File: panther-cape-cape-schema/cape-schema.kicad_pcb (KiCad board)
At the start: 2 copper layers, 86.4 x 54.6 mm, 28 parts, among them P1 OUT2 P4, P10 Y_SENSORS, P11 SENSORS+, P12 SENSORS-, P13 SPINCLE_FEEDBACK, P14 SPINDLE, P15 Z_SENSORS, P16 DRIVER_ENABLE_SWITCH, P17 DRIVER_X, P18 DRIVER_Y, P19 DRIVER_Z, P2 IN2 P2, P20 DRIVER_ENABLE, P21 X_ALARM, P22 Y/Z_ALARM, P3 POWER_SUPPLY, P4 OUT1 P3, P5 EMERGENCY_STOP_SWITCH, P6 IN1 P1, P7 Z_PROBE_LIMIT_SWITCH, P8 X_SENSORS, P9 X_HOME

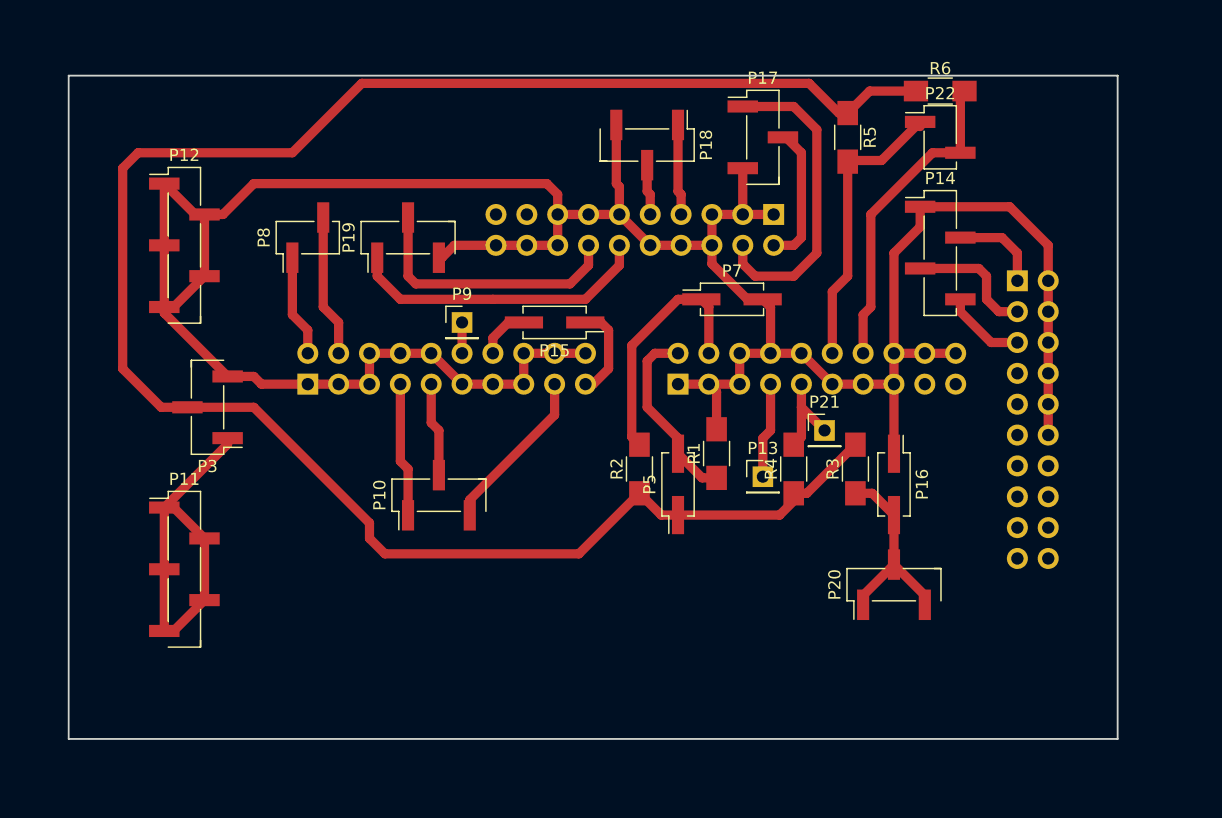
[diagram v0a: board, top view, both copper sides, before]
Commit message: routed single layer pcb
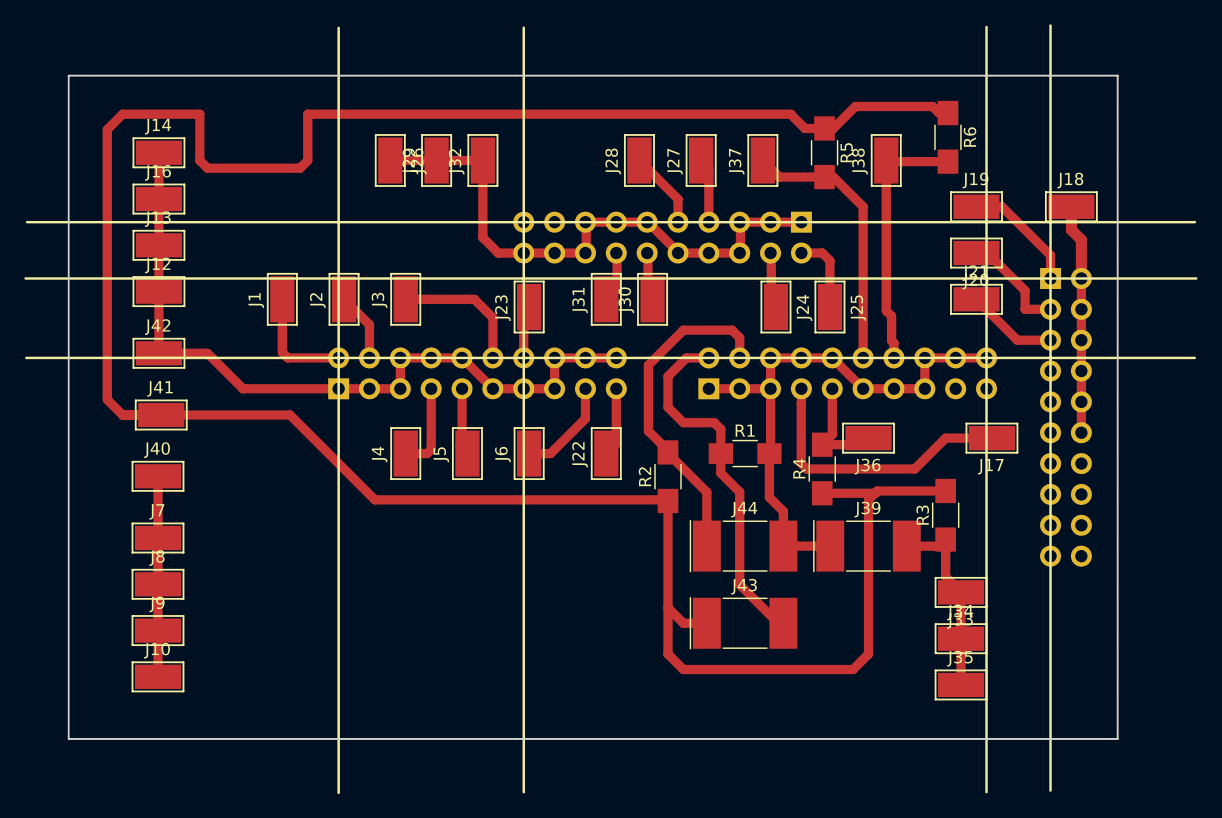
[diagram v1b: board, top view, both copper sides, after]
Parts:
- removed P10: Y_SENSORS, Pin_Headers:Pin_Header_Straight_1x03_Pitch2.54mm_SMD_Pin1Left
- removed P11: SENSORS+, Pin_Headers:Pin_Header_Straight_1x05_Pitch2.54mm_SMD_Pin1Left
- removed P12: SENSORS-, Pin_Headers:Pin_Header_Straight_1x05_Pitch2.54mm_SMD_Pin1Left
- removed P13: SPINCLE_FEEDBACK, Pin_Headers:Pin_Header_Straight_1x01_Pitch2.54mm
- removed P14: SPINDLE, Pin_Headers:Pin_Header_Straight_1x04_Pitch2.54mm_SMD_Pin1Left
- removed P15: Z_SENSORS, Pin_Headers:Pin_Header_Straight_2x01_Pitch2.54mm_SMD
- removed P16: DRIVER_ENABLE_SWITCH, Pin_Headers:Pin_Header_Straight_2x01_Pitch2.54mm_SMD
- removed P17: DRIVER_X, Pin_Headers:Pin_Header_Straight_1x03_Pitch2.54mm_SMD_Pin1Left
- removed P18: DRIVER_Y, Pin_Headers:Pin_Header_Straight_1x03_Pitch2.54mm_SMD_Pin1Left
- removed P19: DRIVER_Z, Pin_Headers:Pin_Header_Straight_1x03_Pitch2.54mm_SMD_Pin1Left
- removed P20: DRIVER_ENABLE, Pin_Headers:Pin_Header_Straight_1x03_Pitch2.54mm_SMD_Pin1Left
- removed P21: X_ALARM, Pin_Headers:Pin_Header_Straight_1x01_Pitch2.54mm
- removed P22: Y/Z_ALARM, Pin_Headers:Pin_Header_Straight_1x02_Pitch2.54mm_SMD_Pin1Left
- removed P3: POWER_SUPPLY, Pin_Headers:Pin_Header_Straight_1x03_Pitch2.54mm_SMD_Pin1Left
- removed P5: EMERGENCY_STOP_SWITCH, Pin_Headers:Pin_Header_Straight_2x01_Pitch2.54mm_SMD
- removed P7: Z_PROBE_LIMIT_SWITCH, Pin_Headers:Pin_Header_Straight_2x01_Pitch2.54mm_SMD
- removed P8: X_SENSORS, Pin_Headers:Pin_Header_Straight_1x02_Pitch2.54mm_SMD_Pin1Left
- removed P9: X_HOME, Pin_Headers:Pin_Header_Straight_1x01_Pitch2.54mm
- added J1: X_LIMIT_MIN, Measurement_Points:Test_Point_Keystone_5019_Minature, F.Cu at (46.2, 133.3)
- added J10: SENSORS+, Measurement_Points:Test_Point_Keystone_5019_Minature, F.Cu at (35.9, 164.4)
- added J12: SENSORS-, Measurement_Points:Test_Point_Keystone_5019_Minature, F.Cu at (36.0, 132.7)
- added J13: SENSORS-, Measurement_Points:Test_Point_Keystone_5019_Minature, F.Cu at (36.0, 128.9)
- added J14: SENSORS-, Measurement_Points:Test_Point_Keystone_5019_Minature, F.Cu at (36.0, 121.3)
- added J16: SENSORS-, Measurement_Points:Test_Point_Keystone_5019_Minature, F.Cu at (36.0, 125.1)
- added J17: SPINDLE_FEEDBACK, Measurement_Points:Test_Point_Keystone_5019_Minature, F.Cu at (104.6, 144.8)
- added J18: SPINDLE_SIGNAL-, Measurement_Points:Test_Point_Keystone_5019_Minature, F.Cu at (111.1, 125.7)
- added J19: SPINDLE_ENABLE, Measurement_Points:Test_Point_Keystone_5019_Minature, F.Cu at (103.3, 125.7)
- added J2: X_LIMIT_MAX, Measurement_Points:Test_Point_Keystone_5019_Minature, F.Cu at (51.2, 133.3)
- added J20: SPINDLE_DIR, Measurement_Points:Test_Point_Keystone_5019_Minature, F.Cu at (103.3, 129.5)
- added J21: SPINDLE_RPM, Measurement_Points:Test_Point_Keystone_5019_Minature, F.Cu at (103.3, 133.3)
- added J22: Z_LIMIT_MIN, Measurement_Points:Test_Point_Keystone_5019_Minature, F.Cu at (72.8, 146.1)
- added J23: Z_LIMIT_MAX, Measurement_Points:Test_Point_Keystone_5019_Minature, F.Cu at (66.5, 134.0)
- added J24: X_DIR, Measurement_Points:Test_Point_Keystone_5019_Minature, F.Cu at (86.8, 134.0)
- added J25: X_STEP, Measurement_Points:Test_Point_Keystone_5019_Minature, F.Cu at (91.2, 134.0)
- added J26: DRIVER_SIGNALS-, Measurement_Points:Test_Point_Keystone_5019_Minature, F.Cu at (55.1, 121.9)
- added J27: Y_DIR, Measurement_Points:Test_Point_Keystone_5019_Minature, F.Cu at (80.6, 121.9)
- added J28: Y_STEP, Measurement_Points:Test_Point_Keystone_5019_Minature, F.Cu at (75.6, 121.9)
- added J29: DRIVER_SIGNALS-, Measurement_Points:Test_Point_Keystone_5019_Minature, F.Cu at (58.9, 121.9)
- added J3: X_HOME, Measurement_Points:Test_Point_Keystone_5019_Minature, F.Cu at (56.3, 133.3)
- added J30: Z_DIR, Measurement_Points:Test_Point_Keystone_5019_Minature, F.Cu at (76.6, 133.3)
- added J31: Z_STEP, Measurement_Points:Test_Point_Keystone_5019_Minature, F.Cu at (72.8, 133.3)
- added J32: DRIVER_SIGNALS-, Measurement_Points:Test_Point_Keystone_5019_Minature, F.Cu at (62.7, 121.9)
- added J33: DRIVER_ENABLE, Measurement_Points:Test_Point_Keystone_5019_Minature, F.Cu at (102.0, 157.5)
- added J34: DRIVER_ENABLE, Measurement_Points:Test_Point_Keystone_5019_Minature, F.Cu at (102.0, 161.3)
- added J35: DRIVER_ENABLE, Measurement_Points:Test_Point_Keystone_5019_Minature, F.Cu at (102.0, 165.1)
- added J36: X_ALARM, Measurement_Points:Test_Point_Keystone_5019_Minature, F.Cu at (94.4, 144.8)
- added J37: Y_ALARM, Measurement_Points:Test_Point_Keystone_5019_Minature, F.Cu at (85.7, 121.9)
- added J38: Z_ALARM, Measurement_Points:Test_Point_Keystone_5019_Minature, F.Cu at (95.9, 121.9)
- added J39: DRIVER_ENABLE_SWITCH, Crystals:Crystal_SMD_MicroCrystal_CC1V-T1A-2pin_8.0x3.7mm, F.Cu at (94.4, 153.7)
- added J4: Y_LIMIT_MIN, Measurement_Points:Test_Point_Keystone_5019_Minature, F.Cu at (56.3, 146.1)
- added J40: SENSORS+, Measurement_Points:Test_Point_Keystone_5019_Minature, F.Cu at (35.9, 147.9)
- added J41: PC+, Measurement_Points:Test_Point_Keystone_5019_Minature, F.Cu at (36.2, 142.9)
- added J42: GND, Measurement_Points:Test_Point_Keystone_5019_Minature, F.Cu at (36.0, 137.8)
- added J43: EMERGENCY_STOP_SWITCH, Crystals:Crystal_SMD_MicroCrystal_CC1V-T1A-2pin_8.0x3.7mm, F.Cu at (84.3, 160.0)
- added J44: Z_PROBE_LIMIT_SWITCH, Crystals:Crystal_SMD_MicroCrystal_CC1V-T1A-2pin_8.0x3.7mm, F.Cu at (84.3, 153.7)
- added J5: Y_LIMIT_MAX, Measurement_Points:Test_Point_Keystone_5019_Minature, F.Cu at (61.4, 146.1)
- added J6: Y_HOME, Measurement_Points:Test_Point_Keystone_5019_Minature, F.Cu at (66.5, 146.1)
- added J7: SENSORS+, Measurement_Points:Test_Point_Keystone_5019_Minature, F.Cu at (35.9, 153.0)
- added J8: SENSORS+, Measurement_Points:Test_Point_Keystone_5019_Minature, F.Cu at (35.9, 156.8)
- added J9: SENSORS+, Measurement_Points:Test_Point_Keystone_5019_Minature, F.Cu at (35.9, 160.6)
- moved R3 8.35 mm to (100.8, 151.1)
- moved R6 3.86 mm to (101.0, 120.0), turned to 270 degrees
- moved P1 2.74 mm to (109.4, 131.6)
- moved P2 2.57 mm to (81.3, 140.7)
- moved P6 2.57 mm to (50.8, 140.7)
- moved R2 2.43 mm to (77.9, 148.0)
- moved P4 2.37 mm to (88.9, 127.0)
- moved R4 2.35 mm to (90.6, 147.3)
- moved R1 2.35 mm to (84.3, 146.1), turned to 0 degrees
- moved R5 2.29 mm to (90.8, 121.3)
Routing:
- net DRIVER_SIGNALS-: track 236.0 -> 175.1 mm
- net PC+: track 159.7 -> 212.0 mm
- net X_DIR: track 25.9 -> 4.60 mm
- net Z_STEP: track 25.1 -> 3.97 mm
- net Z_DIR: track 22.2 -> 4.18 mm
- net SPINDLE_RPM_FEEDBACK: track 7.88 -> 23.1 mm
- net SENSORS+: track 31.8 -> 17.0 mm
- net EMERGENCY_STOP: track 15.5 -> 30.0 mm
- net X_HOME: track 2.54 -> 11.1 mm
- net Z_PROBE: track 20.4 -> 27.5 mm
- net X_LIMIT_MAX: track 11.7 -> 5.69 mm
- net Y_HOME: track 13.7 -> 8.29 mm
- net X_STEP: track 11.6 -> 6.36 mm
- net Z_ALARM: track 26.4 -> 21.6 mm
- net Y_LIMIT_MIN: track 11.1 -> 7.23 mm
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- added copper zone on F.Cu, net DRIVER_SIGNALS-

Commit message: added mounting holes
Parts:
- added REF**: 1pin, Connectors:1pin, F.Cu at (109.2, 121.3)
- added REF**: 1pin, Connectors:1pin, F.Cu at (109.2, 163.2)
- added REF**: 1pin, Connectors:1pin, F.Cu at (43.2, 166.4)
- added REF**: 1pin, Connectors:1pin, F.Cu at (43.2, 118.1)
- moved J14 8.92 mm to (40.6, 128.9)
- moved J18 1.42 mm to (111.8, 127.0)
- moved J10 1.27 mm to (34.7, 164.4)
- moved J12 1.27 mm to (34.7, 132.7)
- moved J13 1.27 mm to (34.7, 128.9)
- moved J16 1.27 mm to (34.7, 125.1)
- moved J40 1.27 mm to (34.7, 147.9)
- moved J41 1.27 mm to (34.9, 142.9)
- moved J42 1.27 mm to (34.7, 137.8)
- moved J7 1.27 mm to (34.7, 153.0)
- moved J8 1.27 mm to (34.7, 156.8)
- moved J9 1.27 mm to (34.7, 160.6)
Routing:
- net PC+: track 212.0 -> 208.1 mm
- net DRIVER_SIGNALS-: track 175.1 -> 175.7 mm

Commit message: added missing footprint library
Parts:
- P1, P2, P4, P6: footprint Socket_Strips:Socket_Strip_Straight_2x10 -> conn20-small-drills:Socket_Strip_Straight_2x10
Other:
- net class Default: clearance 0.5 -> 0
- rule trace_clearance: 0.5 -> 0

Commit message: fixed connector naming mismatch
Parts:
- J27: value Y_DIR -> Y_STEP
- J28: value Y_STEP -> Y_DIR
- J30: value Z_DIR -> Z_STEP
- J31: value Z_STEP -> Z_DIR
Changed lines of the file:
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@@
   )
   (layers
-    (0 F.Cu signal)
-    (31 B.Cu signal)
-    (32 B.Adhes user)
-    (33 F.Adhes user)
+    (0 F.Cu signal hide)
+    (31 B.Cu signal hide)
+    (32 B.Adhes user hide)
+    (33 F.Adhes user hide)
     (34 B.Paste user)
     (35 F.Paste user)
@@
     (46 B.CrtYd user)
     (47 F.CrtYd user)
-    (48 B.Fab user)
+    (48 B.Fab user hide)
     (49 F.Fab user)
   )
@@
   (net 26 DRIVER_ENABLE)
   (net 27 SENSORS+)
-  (net_class Default "This is the default net class."
+  (net_class Default "Dies ist die voreingestellte Netzklasse."
     (clearance 0)
     (trace_width 0.25)
@@
       (effects (font (size 1 1) (thickness 0.15)))
     )
-    (fp_text value Y_DIR (at 0 2.25 90) (layer F.Fab)
+    (fp_text value Y_STEP (at 0 2.25 90) (layer F.Fab)
       (effects (font (size 1 1) (thickness 0.15)))
     )
@@
       (effects (font (size 1 1) (thickness 0.15)))
     )
-    (fp_text value Y_STEP (at 0 2.25 90) (layer F.Fab)
+    (fp_text value Y_DIR (at 0 2.25 90) (layer F.Fab)
       (effects (font (size 1 1) (thickness 0.15)))
     )
@@
       (effects (font (size 1 1) (thickness 0.15)))
     )
-    (fp_text value Z_DIR (at 0 2.25 90) (layer F.Fab)
+    (fp_text value Z_STEP (at 0 2.25 90) (layer F.Fab)
       (effects (font (size 1 1) (thickness 0.15)))
     )
@@
       (effects (font (size 1 1) (thickness 0.15)))
     )
-    (fp_text value Z_STEP (at 0 2.25 90) (layer F.Fab)
-      (effects (font (size 1 1) (thickness 0.15)))
-    )
+    (fp_text value Z_DIR (at 0 2.25 90) (layer F.Fab)
+      (effects (font (size 1 1) (thickness 0.15)))
+    )
